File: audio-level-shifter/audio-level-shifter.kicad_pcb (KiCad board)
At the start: 2 copper layers, 53.3 x 17.8 mm, 11 parts, among them J1 IN, J2 OUT

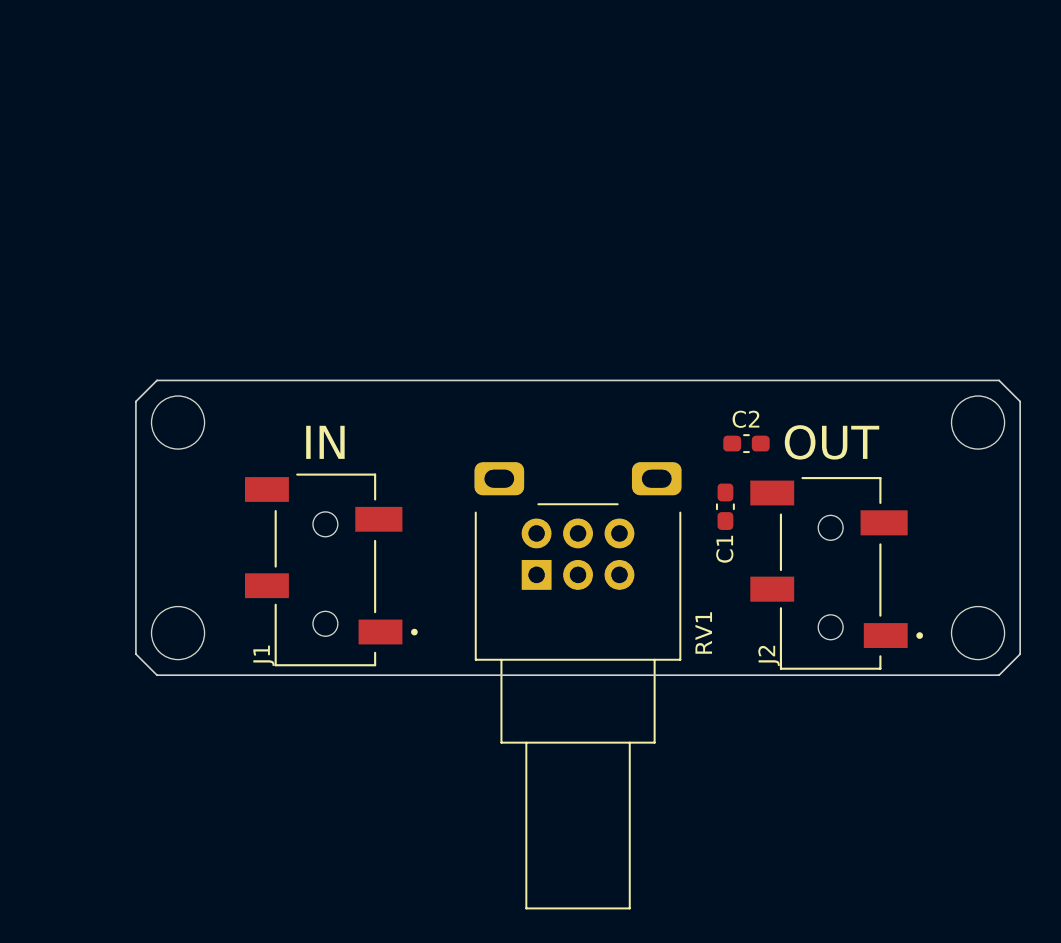
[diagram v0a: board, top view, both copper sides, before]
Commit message: Add 3D models for the pot and 3.5mm audio socket; wire up circuit on the PCB.  Part of #3
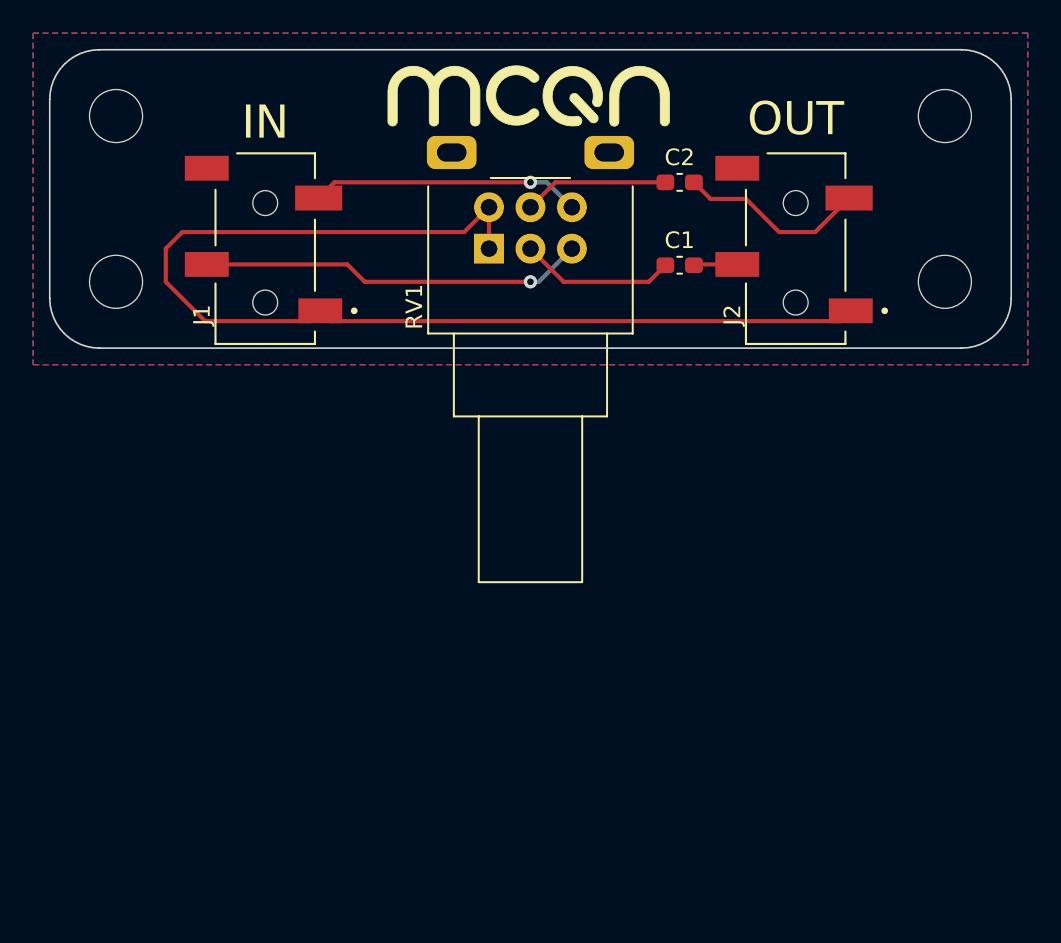
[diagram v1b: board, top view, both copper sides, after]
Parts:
- C1, C2: value C_Small -> 0.1uF
- moved REF** 24.7 mm to (80.0, 102.5)
- moved REF** 22.8 mm to (80.0, 95.0)
- moved H1 21.5 mm to (75.0, 102.0)
- moved H2 21.3 mm to (125.0, 102.0)
- moved RV1 19.9 mm to (97.5, 100.0)
- moved J1 19.7 mm to (84.0, 100.0)
- moved J2 19.7 mm to (116.0, 100.0)
- moved H3 18.9 mm to (75.0, 92.0)
- moved H4 18.6 mm to (125.0, 92.0)
- moved C2 16.3 mm to (109.0, 96.0)
- moved C1 14.8 mm to (109.0, 101.0), turned to 180 degrees
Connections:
- net Net-(J1-Pad1) renamed GNDA
- RV1 pad 2: Net-(C2-Pad1) -> Net-(C1-Pad2)
- RV1 pad 3: Net-(J1-Pad2) -> Net-(J1-Pad3)
- RV1 pad 5: Net-(C1-Pad2) -> Net-(C2-Pad1)
- RV1 pad 6: Net-(J1-Pad3) -> Net-(J1-Pad2)
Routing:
- net GNDA: track 0.00 -> 68.1 mm
- net Net-(J1-Pad3): track 0.00 -> 23.3 mm, vias 0 -> 1
- net Net-(J1-Pad2): track 0.00 -> 16.3 mm, vias 0 -> 1
- net Net-(C2-Pad2): track 0.00 -> 11.5 mm
- net Net-(C1-Pad2): track 0.00 -> 9.38 mm
- net Net-(C2-Pad1): track 0.00 -> 8.76 mm
- net Net-(C1-Pad1): track 0.00 -> 2.63 mm
- added copper zone on B.Cu, net GNDA
- added copper zone on F.Cu, net GNDA
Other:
- board size 53.3 x 17.8 mm -> 58 x 18 mm
- board text added: "mcqn.com/ibal249"
- board text added: "r20240814"
